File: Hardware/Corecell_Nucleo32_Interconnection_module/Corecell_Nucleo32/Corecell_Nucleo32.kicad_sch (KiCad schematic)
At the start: 29 parts, among them IC1 PCI_EXPRESS_CARD, J1 Conn_02x19_Top_Bottom, J2 Bus Standard, J3 Calculatrice_UART_groove, J4 RAK5146_UART_groove(GPS), J5 RAK5146_I2C_groove(GPS), J6 RAK5146_SPI_groove(MCU), Q1 BC548, U1 ESP32-DEVKITC-32D

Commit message: Footprint assignement is done
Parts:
- C1, C7: footprint (none) -> Capacitor_SMD:C_0603_1608Metric
- C2, C3, C4, C5, C6, C8: footprint (none) -> Capacitor_SMD:C_0402_1005Metric
- J1: footprint (none) -> Connector_PinHeader_2.54mm:PinHeader_2x19_P2.54mm_Vertical
- J2: footprint (none) -> Connector_PinHeader_2.54mm:PinHeader_2x20_P2.54mm_Vertical
- J3: footprint (none) -> Connector_PinSocket_2.54mm:PinSocket_1x04_P2.54mm_Vertical
- J4, J5: footprint (none) -> Connector_PinSocket_2.54mm:PinSocket_1x05_P2.54mm_Vertical
- J6: footprint (none) -> Connector_PinSocket_2.54mm:PinSocket_1x06_P2.54mm_Vertical
- JP1, JP2, JP3: footprint (none) -> Connector_PinHeader_2.54mm:PinHeader_1x02_P2.54mm_Vertical
- R1, R3, R4, R5: footprint (none) -> Jumper:SolderJumper-2_P1.3mm_Bridged2Bar_RoundedPad1.0x1.5mm
- R2, R6, R7, R8, R9: footprint (none) -> Resistor_SMD:R_0402_1005Metric
- U1: footprint MODULE_ESP32-DEVKITC-32D -> ESP32-DEVKITC-32D:MODULE_ESP32-DEVKITC-32D

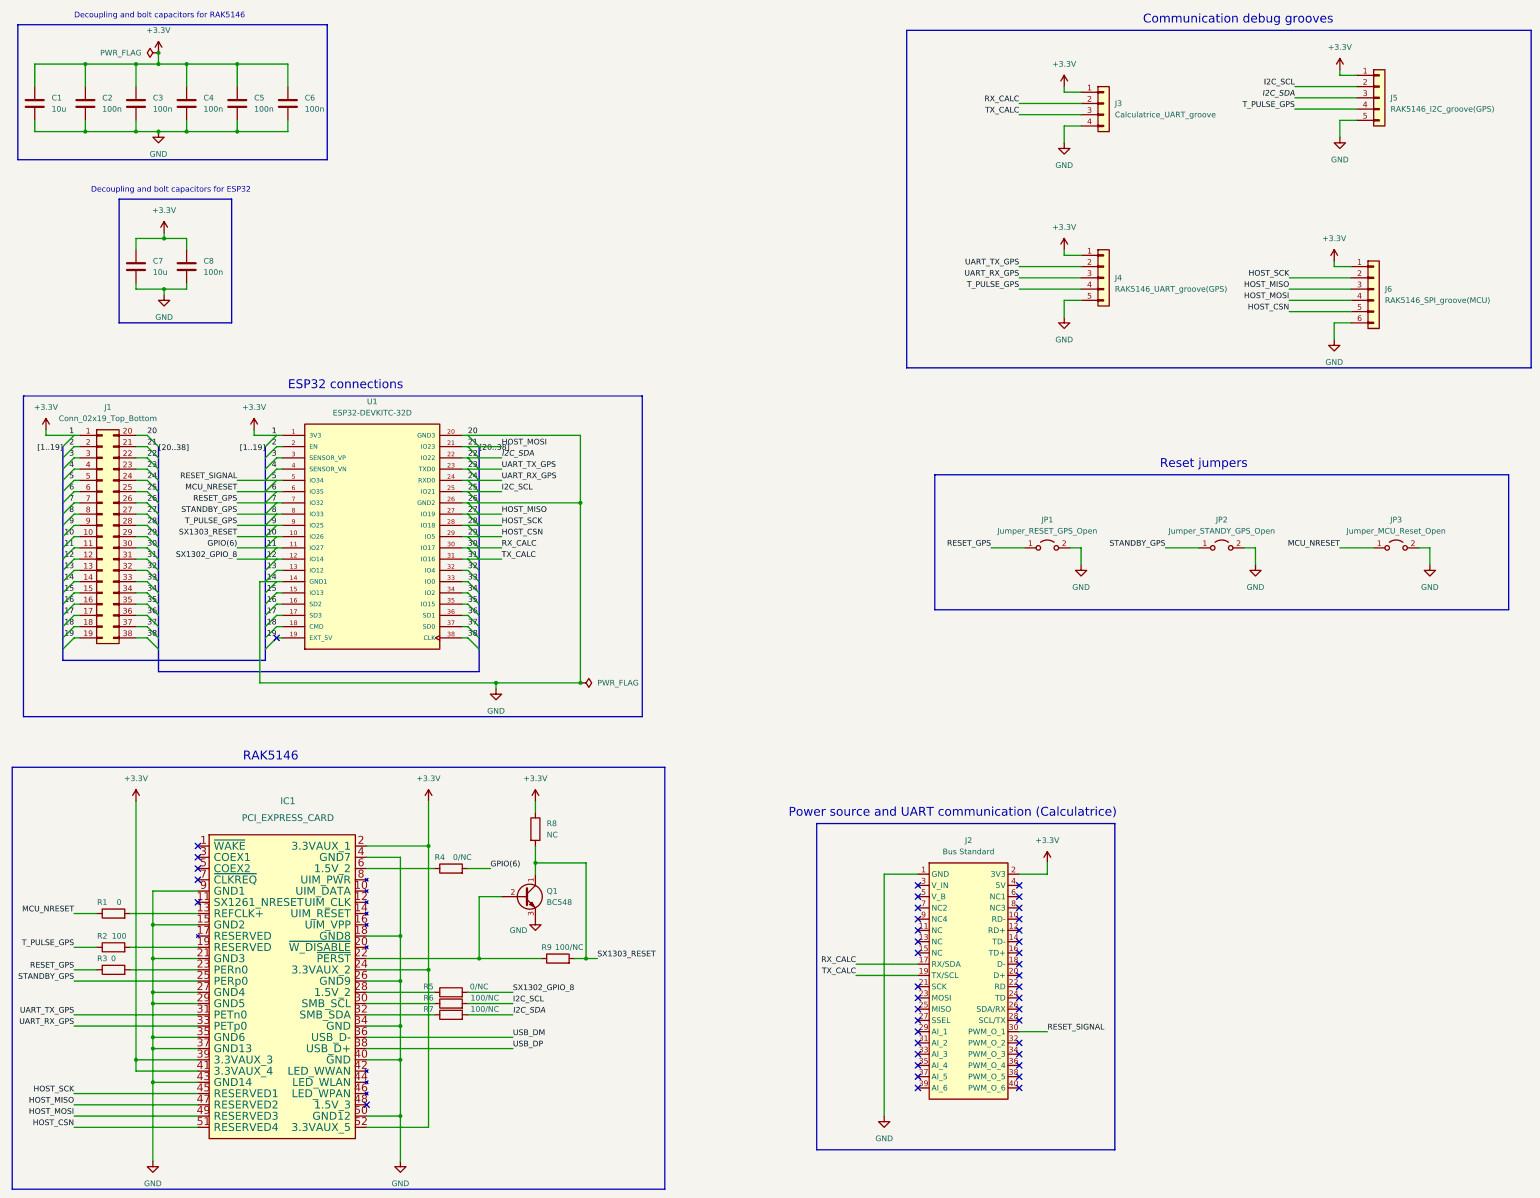
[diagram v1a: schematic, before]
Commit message: Jumpers for esp32 were changed for splited 1x19.
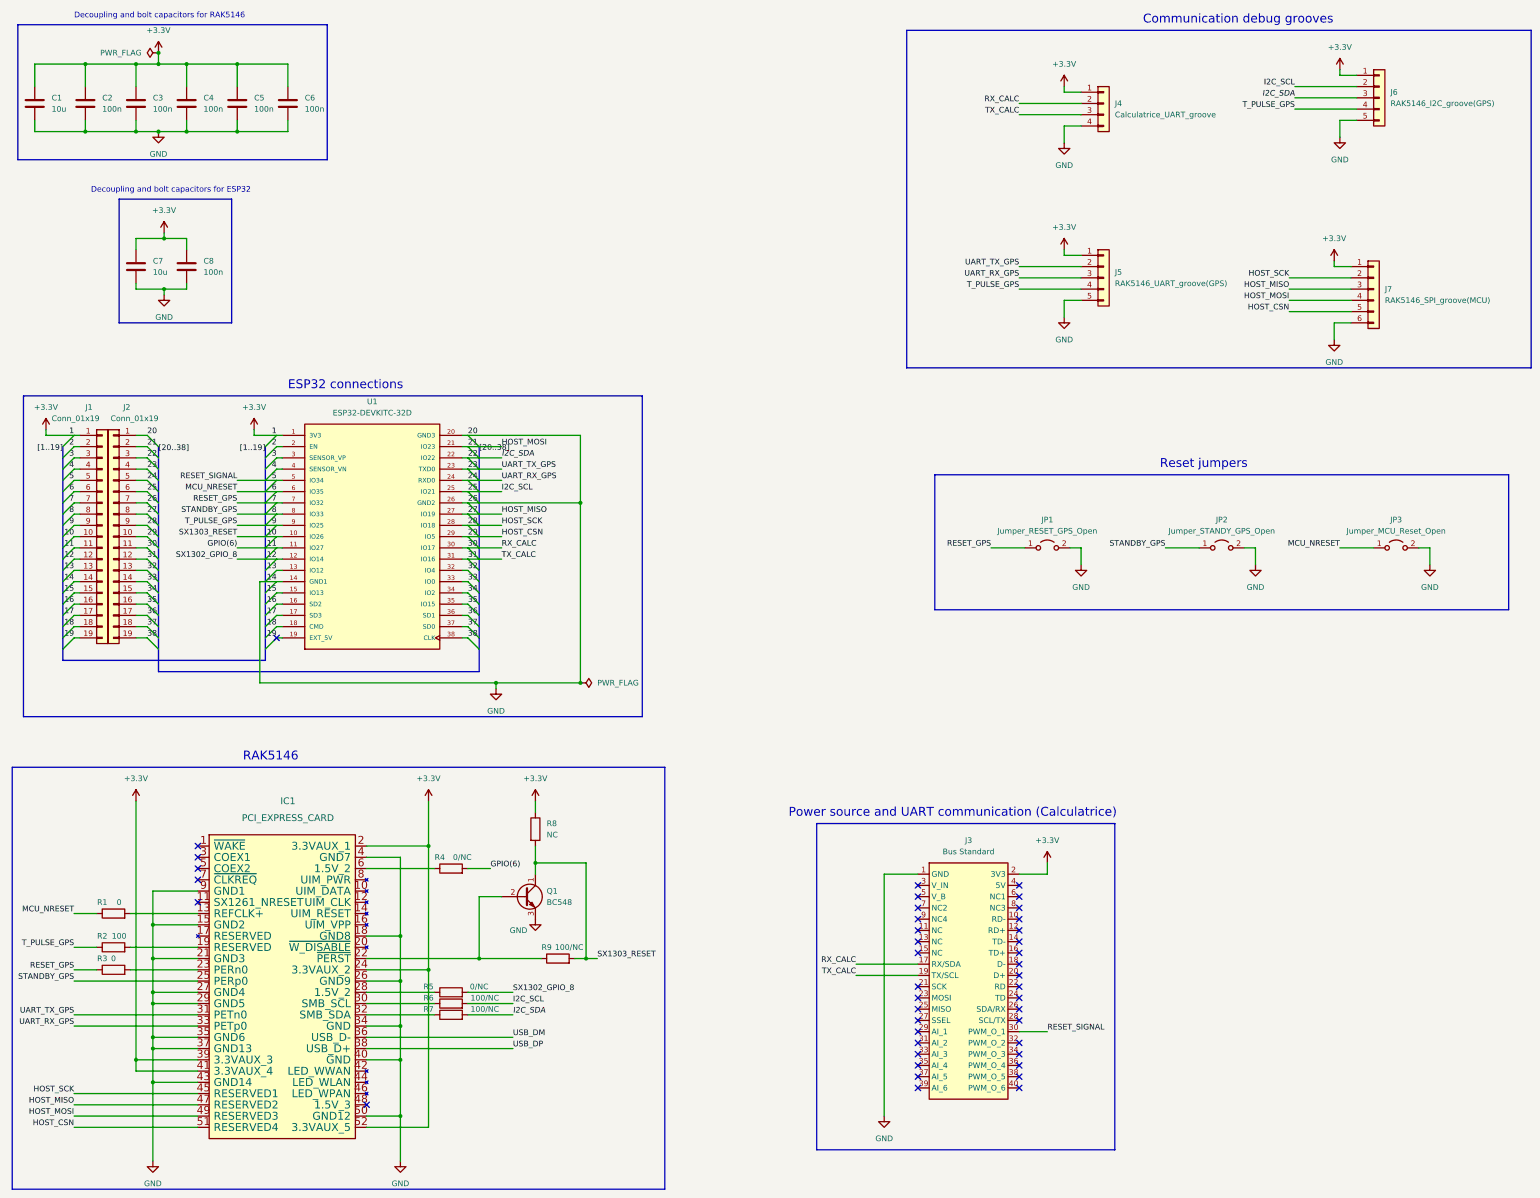
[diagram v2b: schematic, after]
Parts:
- removed J1: Conn_02x19_Top_Bottom, Connector_PinHeader_2.54mm:PinHeader_2x19_P2.54mm_Vertical, symbol Connector_Generic:Conn_02x19_Top_Bottom
- added J1, J2: Conn_01x19, Connector_PinSocket_2.54mm:PinSocket_1x19_P2.54mm_Vertical, symbol Connector_Generic:Conn_01x19
- renumbered J2 to J3, J3 to J4, J4 to J5, J5 to J6, J6 to J7
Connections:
- net +3V3: now also J1.1 (Pin_1)
- net 10: now also J1.10 (Pin_10)
- net 11: now also J1.11 (Pin_11)
- net 12: now also J1.12 (Pin_12)
- net 13: now also J1.13 (Pin_13)
- net 15: now also J1.15 (Pin_15)
- net 16: now also J1.16 (Pin_16)
- net 17: now also J1.17 (Pin_17)
- net 18: now also J1.18 (Pin_18)
- net 19: now also J1.19 (Pin_19)
- net 2: now also J1.2 (Pin_2)
- net 21: now also J2.2 (Pin_2)
- net 22: now also J2.3 (Pin_3)
- net 23: now also J2.4 (Pin_4)
- net 24: now also J2.5 (Pin_5)
- net 25: now also J2.6 (Pin_6)
- net 27: now also J2.8 (Pin_8)
- net 28: now also J2.9 (Pin_9)
- net 29: now also J2.10 (Pin_10)
- net 3: now also J1.3 (Pin_3)
- net 30: now also J2.11 (Pin_11)
- net 31: now also J2.12 (Pin_12)
- net 32: now also J2.13 (Pin_13)
- net 33: now also J2.14 (Pin_14)
- net 34: now also J2.15 (Pin_15)
- net 35: now also J2.16 (Pin_16)
- net 36: now also J2.17 (Pin_17)
- net 37: now also J2.18 (Pin_18)
- net 38: now also J2.19 (Pin_19)
- net 4: now also J1.4 (Pin_4)
- net 5: now also J1.5 (Pin_5)
- net 6: now also J1.6 (Pin_6)
- net 7: now also J1.7 (Pin_7)
- net 8: now also J1.8 (Pin_8)
- net 9: now also J1.9 (Pin_9)
- net GND: now also J1.14 (Pin_14), J2.1 (Pin_1), J2.7 (Pin_7)

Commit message: Some changes in footprint and capacitors value
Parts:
- R1, R3: footprint Jumper:SolderJumper-2_P1.3mm_Bridged2Bar_RoundedPad1.0x1.5mm -> Resistor_SMD:R_0402_1005Metric
- R4, R5: value 0/NC -> 0; footprint Jumper:SolderJumper-2_P1.3mm_Bridged2Bar_RoundedPad1.0x1.5mm -> Resistor_SMD:R_0402_1005Metric
- R6, R7, R9: value 100/NC -> 100
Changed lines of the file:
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@@
     (property "Reference" "R1" (id 0) (at 36.83 217.17 90))
     (property "Value" "0" (id 1) (at 40.64 217.17 90))
-    (property "Footprint" "Jumper:SolderJumper-2_P1.3mm_Bridged2Bar_RoundedPad1.0x1.5mm" (id 2) (at 39.37 221.488 90)
+    (property "Footprint" "Resistor_SMD:R_0402_1005Metric" (id 2) (at 39.37 221.488 90)
       (effects (font (size 1.27 1.27)) hide)
     )
@@
     (in_bom yes) (on_board yes)
     (property "Reference" "R5" (id 0) (at 110.49 236.22 90))
-    (property "Value" "0/NC" (id 1) (at 121.92 236.22 90))
-    (property "Footprint" "Jumper:SolderJumper-2_P1.3mm_Bridged2Bar_RoundedPad1.0x1.5mm" (id 2) (at 115.57 239.268 90)
+    (property "Value" "0" (id 1) (at 121.92 236.22 90))
+    (property "Footprint" "Resistor_SMD:R_0402_1005Metric" (id 2) (at 115.57 239.268 90)
       (effects (font (size 1.27 1.27)) hide)
     )
@@
     (in_bom yes) (on_board yes)
     (property "Reference" "R7" (id 0) (at 110.49 241.3 90))
-    (property "Value" "100/NC" (id 1) (at 123.19 241.3 90))
+    (property "Value" "100" (id 1) (at 123.19 241.3 90))
     (property "Footprint" "Resistor_SMD:R_0402_1005Metric" (id 2) (at 115.57 244.348 90)
       (effects (font (size 1.27 1.27)) hide)
@@
     (in_bom yes) (on_board yes)
     (property "Reference" "R6" (id 0) (at 110.49 238.76 90))
-    (property "Value" "100/NC" (id 1) (at 123.19 238.76 90))
+    (property "Value" "100" (id 1) (at 123.19 238.76 90))
     (property "Footprint" "Resistor_SMD:R_0402_1005Metric" (id 2) (at 115.57 241.808 90)
       (effects (font (size 1.27 1.27)) hide)
@@
     (property "Reference" "R3" (id 0) (at 36.83 229.87 90))
     (property "Value" "0" (id 1) (at 39.37 229.87 90))
-    (property "Footprint" "Jumper:SolderJumper-2_P1.3mm_Bridged2Bar_RoundedPad1.0x1.5mm" (id 2) (at 39.37 234.188 90)
+    (property "Footprint" "Resistor_SMD:R_0402_1005Metric" (id 2) (at 39.37 234.188 90)
       (effects (font (size 1.27 1.27)) hide)
     )
@@
     (in_bom yes) (on_board yes)
     (property "Reference" "R9" (id 0) (at 137.16 227.33 90))
-    (property "Value" "100/NC" (id 1) (at 142.24 227.33 90))
+    (property "Value" "100" (id 1) (at 142.24 227.33 90))
     (property "Footprint" "Resistor_SMD:R_0402_1005Metric" (id 2) (at 139.7 231.648 90)
       (effects (font (size 1.27 1.27)) hide)
@@
     (in_bom yes) (on_board yes)
     (property "Reference" "R4" (id 0) (at 113.03 207.01 90))
-    (property "Value" "0/NC" (id 1) (at 118.11 207.01 90))
-    (property "Footprint" "Jumper:SolderJumper-2_P1.3mm_Bridged2Bar_RoundedPad1.0x1.5mm" (id 2) (at 115.57 211.328 90)
+    (property "Value" "0" (id 1) (at 118.11 207.01 90))
+    (property "Footprint" "Resistor_SMD:R_0402_1005Metric" (id 2) (at 115.57 211.328 90)
       (effects (font (size 1.27 1.27)) hide)
     )
@@
     )
     (path "/10d9975f-9534-48f9-9b97-0f93bac7de38"
-      (reference "R1") (unit 1) (value "0") (footprint "Jumper:SolderJumper-2_P1.3mm_Bridged2Bar_RoundedPad1.0x1.5mm")
+      (reference "R1") (unit 1) (value "0") (footprint "Resistor_SMD:R_0402_1005Metric")
     )
     (path "/bddce3a8-18ef-43d8-aff1-d3f56dba90fb"
@@
     )
     (path "/bd802aa0-39be-4607-98b9-9a01dfda3a85"
-      (reference "R3") (unit 1) (value "0") (footprint "Jumper:SolderJumper-2_P1.3mm_Bridged2Bar_RoundedPad1.0x1.5mm")
+      (reference "R3") (unit 1) (value "0") (footprint "Resistor_SMD:R_0402_1005Metric")
     )
     (path "/dd47c322-e7cb-48e6-a531-d529935c0023"
-      (reference "R4") (unit 1) (value "0/NC") (footprint "Jumper:SolderJumper-2_P1.3mm_Bridged2Bar_RoundedPad1.0x1.5mm")
+      (reference "R4") (unit 1) (value "0") (footprint "Resistor_SMD:R_0402_1005Metric")
     )
     (path "/4fb149b6-59f0-4c3d-8e99-08d4f13ff6cb"
-      (reference "R5") (unit 1) (value "0/NC") (footprint "Jumper:SolderJumper-2_P1.3mm_Bridged2Bar_RoundedPad1.0x1.5mm")
+      (reference "R5") (unit 1) (value "0") (footprint "Resistor_SMD:R_0402_1005Metric")
     )
     (path "/88c93c14-7c18-446b-86ea-1733c1240d15"
-      (reference "R6") (unit 1) (value "100/NC") (footprint "Resistor_SMD:R_0402_1005Metric")
+      (reference "R6") (unit 1) (value "100") (footprint "Resistor_SMD:R_0402_1005Metric")
     )
     (path "/74a3f835-1688-4232-afdf-d78f26dac9f6"
-      (reference "R7") (unit 1) (value "100/NC") (footprint "Resistor_SMD:R_0402_1005Metric")
+      (reference "R7") (unit 1) (value "100") (footprint "Resistor_SMD:R_0402_1005Metric")
     )
     (path "/277600d8-d71e-4ec8-ba87-68ddff6527b0"
@@
     )
     (path "/c12c61c0-e74f-42fe-a226-12f19abc5699"
-      (reference "R9") (unit 1) (value "100/NC") (footprint "Resistor_SMD:R_0402_1005Metric")
+      (reference "R9") (unit 1) (value "100") (footprint "Resistor_SMD:R_0402_1005Metric")
     )
     (path "/1afd857d-443e-4f1d-a6f8-c083b19098f3"

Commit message: The reset jumpers were changed the footprint for a push button.
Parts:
- JP1, JP2, JP3: footprint Connector_PinHeader_2.54mm:PinHeader_1x02_P2.54mm_Vertical -> Button_Switch_SMD:SW_Push_1P1T_NO_CK_KMR2
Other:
- note added: "Reset button"
- note removed: "Reset jumpers"
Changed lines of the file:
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@@
     (effects (font (size 2 2)) (justify left bottom))
   )
-  (text "Reset jumpers\n" (at 275.59 119.38 0)
+  (text "Reset button\n" (at 275.59 119.38 0)
     (effects (font (size 2 2)) (justify left bottom))
   )
@@
     (property "Reference" "JP3" (id 0) (at 328.93 130.81 0))
     (property "Value" "Jumper_MCU_Reset_Open" (id 1) (at 328.93 133.35 0))
-    (property "Footprint" "Connector_PinHeader_2.54mm:PinHeader_1x02_P2.54mm_Vertical" (id 2) (at 328.93 137.16 0)
+    (property "Footprint" "Button_Switch_SMD:SW_Push_1P1T_NO_CK_KMR2" (id 2) (at 328.93 137.16 0)
       (effects (font (size 1.27 1.27)) hide)
     )
@@
     (property "Reference" "JP2" (id 0) (at 289.56 130.81 0))
     (property "Value" "Jumper_STANDY_GPS_Open" (id 1) (at 289.56 133.35 0))
-    (property "Footprint" "Connector_PinHeader_2.54mm:PinHeader_1x02_P2.54mm_Vertical" (id 2) (at 289.56 137.16 0)
+    (property "Footprint" "Button_Switch_SMD:SW_Push_1P1T_NO_CK_KMR2" (id 2) (at 289.56 137.16 0)
       (effects (font (size 1.27 1.27)) hide)
     )
@@
     (property "Reference" "JP1" (id 0) (at 250.19 130.81 0))
     (property "Value" "Jumper_RESET_GPS_Open" (id 1) (at 250.19 133.35 0))
-    (property "Footprint" "Connector_PinHeader_2.54mm:PinHeader_1x02_P2.54mm_Vertical" (id 2) (at 250.19 137.16 0)
+    (property "Footprint" "Button_Switch_SMD:SW_Push_1P1T_NO_CK_KMR2" (id 2) (at 250.19 137.16 0)
       (effects (font (size 1.27 1.27)) hide)
     )
@@
     )
     (path "/b9905870-ff76-45f2-986e-d6a250ecc088"
-      (reference "JP1") (unit 1) (value "Jumper_RESET_GPS_Open") (footprint "Connector_PinHeader_2.54mm:PinHeader_1x02_P2.54mm_Vertical")
+      (reference "JP1") (unit 1) (value "Jumper_RESET_GPS_Open") (footprint "Button_Switch_SMD:SW_Push_1P1T_NO_CK_KMR2")
     )
     (path "/7bedfbfb-5f5d-4a06-8921-aa55997b07ca"
-      (reference "JP2") (unit 1) (value "Jumper_STANDY_GPS_Open") (footprint "Connector_PinHeader_2.54mm:PinHeader_1x02_P2.54mm_Vertical")
+      (reference "JP2") (unit 1) (value "Jumper_STANDY_GPS_Open") (footprint "Button_Switch_SMD:SW_Push_1P1T_NO_CK_KMR2")
     )
     (path "/045a038b-a69b-4316-b8fe-886cee7568b8"
-      (reference "JP3") (unit 1) (value "Jumper_MCU_Reset_Open") (footprint "Connector_PinHeader_2.54mm:PinHeader_1x02_P2.54mm_Vertical")
+      (reference "JP3") (unit 1) (value "Jumper_MCU_Reset_Open") (footprint "Button_Switch_SMD:SW_Push_1P1T_NO_CK_KMR2")
     )
     (path "/c520be4c-2d19-4f07-9435-cdcabfb6b7b4"
